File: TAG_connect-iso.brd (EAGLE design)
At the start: 32.1 x 14.6 mm, 9 parts, among them J2 RJ11-6PTH, U2 ISO7231C_DW_16

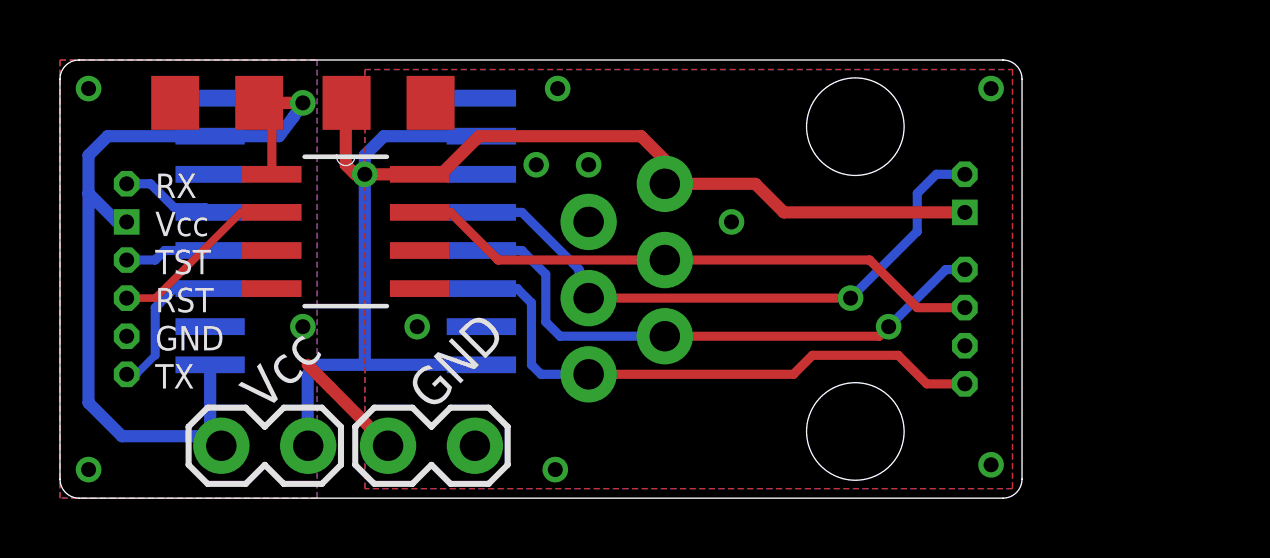
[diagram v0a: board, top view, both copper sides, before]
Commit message: bug fixes
updated iso board to new pinout and rj-12 connector
cleaned up safe-msp board
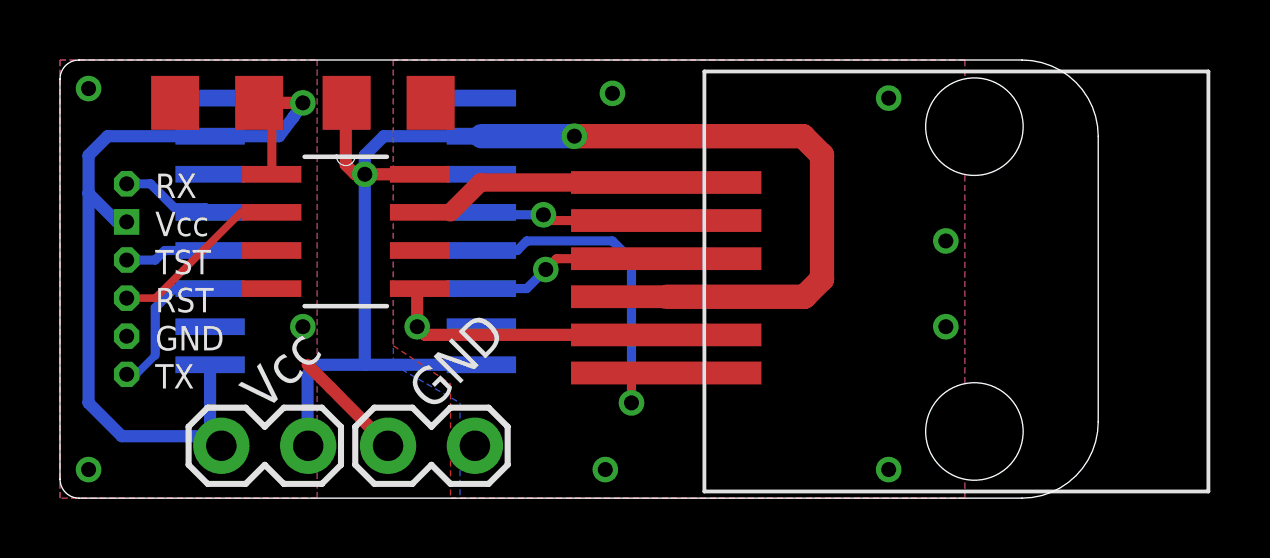
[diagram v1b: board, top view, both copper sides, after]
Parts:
- removed J2: RJ11-6PTH, SparkFun-Connectors:RJ11-6
- removed U$5: 6-PIN-ICSPSAFE-MSP, LaunchFET:SAFEMSP-6PIN
- added U$1: RJ-12SMD, LaunchFET:MOLEX_RJ45_SMD
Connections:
- net GND_TARGET: now also U$1.GND; no longer J2.5, U$5.GND
- net RESET_TARGET: now also U$1.RST; no longer J2.4, U$5.RST
- net RX_TARGET: now also U$1.RX; no longer J2.3, U$5.RX
- net TEST_TARGET: now also U$1.TEST; no longer J2.2, U$5.TST
- net TX_TARGET: now also U$1.TX; no longer J2.1, U$5.TX
- net VCC_TARGET: now also U$1.VCC; no longer J2.6, U$5.VCC
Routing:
- net RX_TARGET: track 20.1 -> 6.28 mm
- net TX_TARGET: track 19.2 -> 6.58 mm, vias 0 -> 1
- net RESET_TARGET: track 19.5 -> 8.63 mm
- net GND_TARGET: track 0.00 -> 9.72 mm, vias 8 -> 7
- net TEST_TARGET: track 19.2 -> 12.3 mm
- net VCC_TARGET: track 44.3 -> 46.0 mm, vias 1 -> 2
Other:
- board size 32.1 x 14.6 mm -> 34.6 x 14.6 mm
